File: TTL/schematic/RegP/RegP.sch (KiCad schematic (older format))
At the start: 23 parts, among them U1 74LS153, U10 74LS32, U2 74LS153, U3 74LS175, U4 74LS32, U5 74LS08, U6 74LS08, U8 74LS86, U9 74LS32

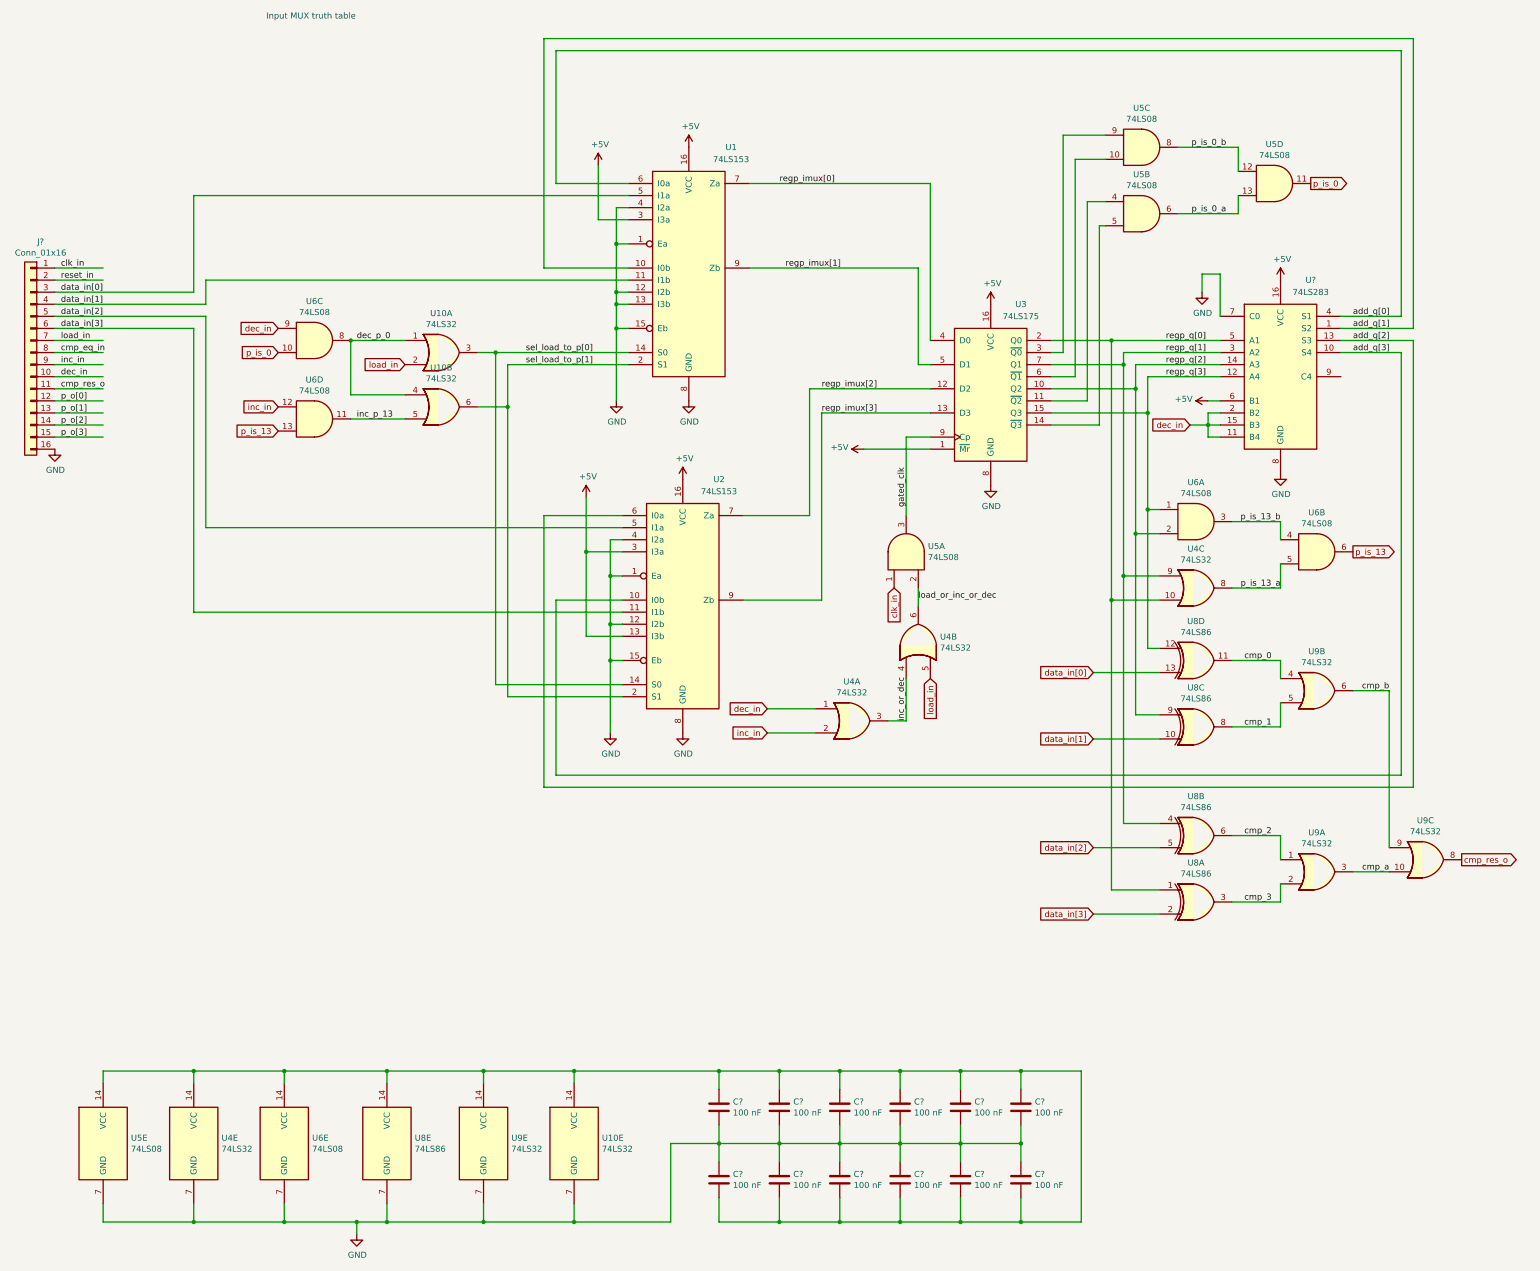
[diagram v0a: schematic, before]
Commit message: Added docu, work in progress schematics and vhdl
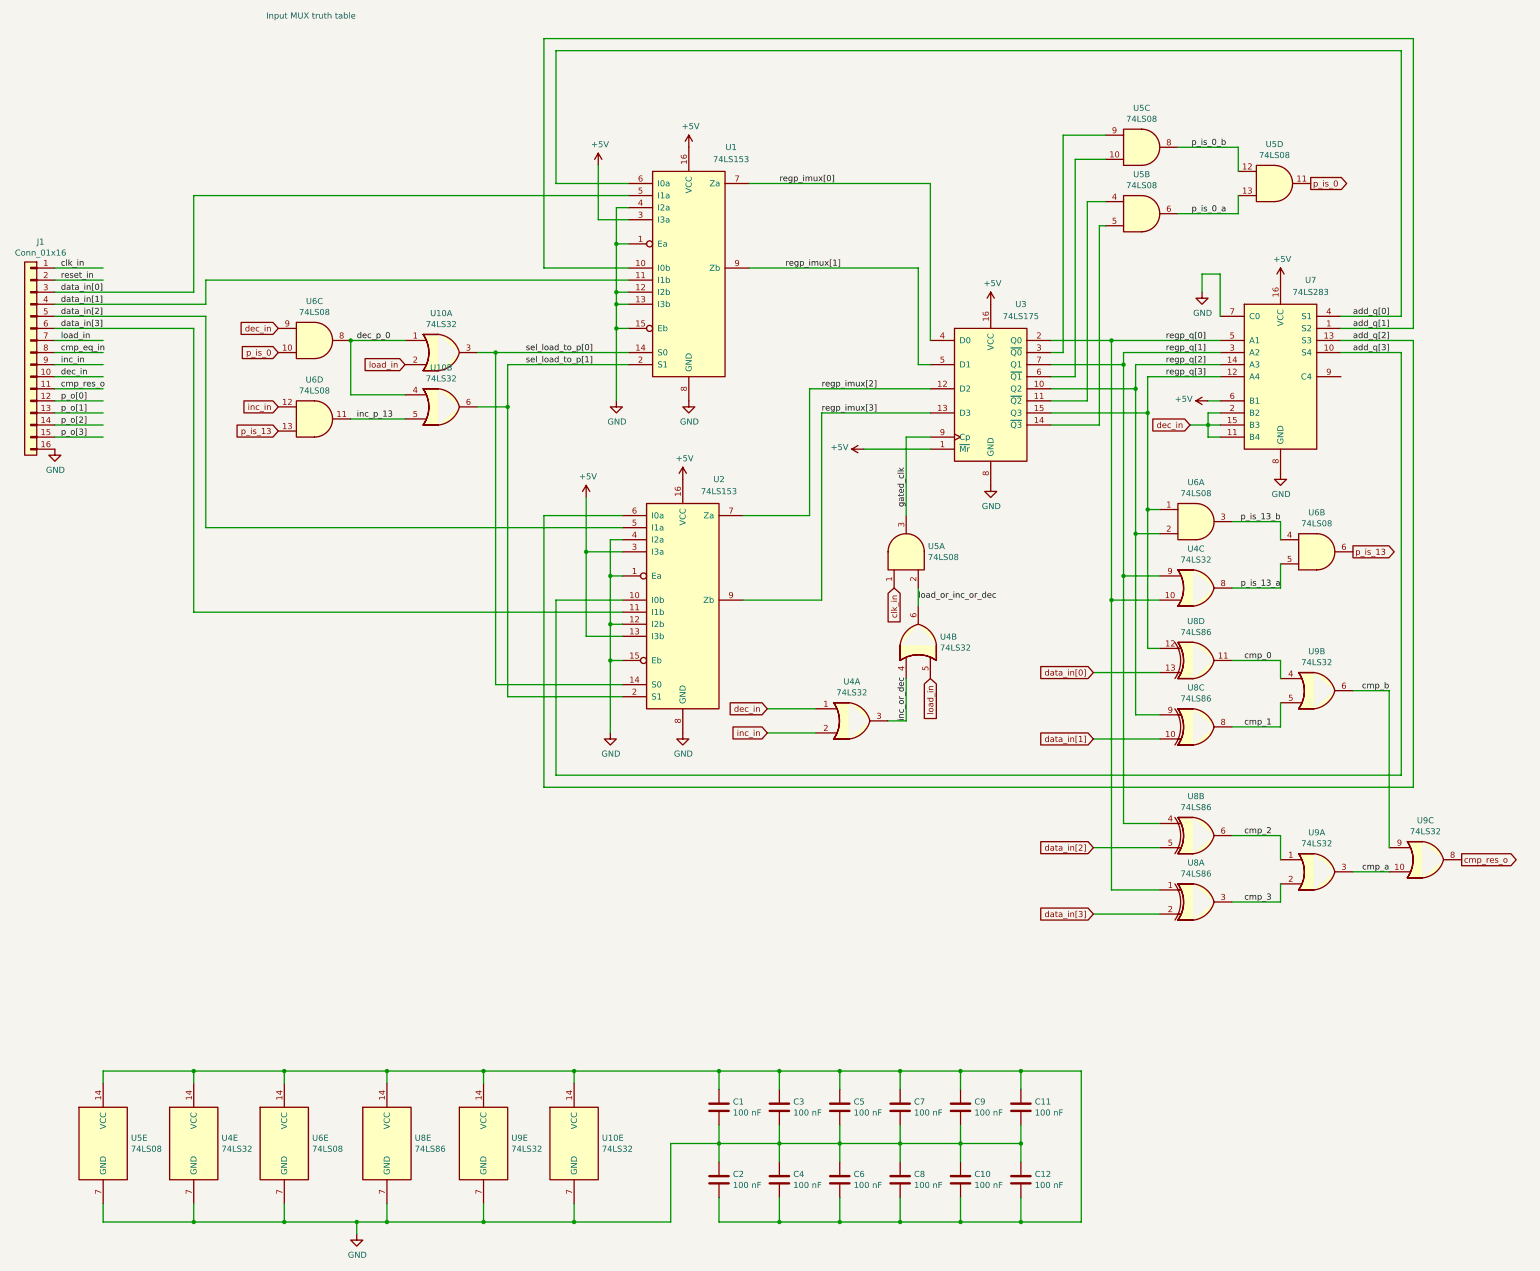
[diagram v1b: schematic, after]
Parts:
- gave numbers to parts that had none: 14
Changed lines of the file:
@@
 $EndComp
 $Comp
-L 74xx:74LS283 U?
+L 74xx:74LS283 U7
 U 1 1 609CD38B
 P 11100 3800
-F 0 "U?" H 11350 4600 50  0000 C CNN
+F 0 "U7" H 11350 4600 50  0000 C CNN
 F 1 "74LS283" H 11350 4500 50  0000 C CNN
 F 2 "" H 11100 3800 50  0001 C CNN
@@
 	10000 3800 10600 3800
 $Comp
-L power:GND #PWR?
+L power:GND #PWR0101
 U 1 1 609CF019
 P 8700 4700
-F 0 "#PWR?" H 8700 4450 50  0001 C CNN
+F 0 "#PWR0101" H 8700 4450 50  0001 C CNN
 F 1 "GND" H 8705 4527 50  0000 C CNN
 F 2 "" H 8700 4700 50  0001 C CNN
@@
 $EndComp
 $Comp
-L power:GND #PWR?
+L power:GND #PWR0102
 U 1 1 609CF0EF
 P 11100 4600
-F 0 "#PWR?" H 11100 4350 50  0001 C CNN
+F 0 "#PWR0102" H 11100 4350 50  0001 C CNN
 F 1 "GND" H 11105 4427 50  0000 C CNN
 F 2 "" H 11100 4600 50  0001 C CNN
@@
 $EndComp
 $Comp
-L power:+5V #PWR?
+L power:+5V #PWR0103
 U 1 1 609D0CA6
 P 8700 3200
-F 0 "#PWR?" H 8700 3050 50  0001 C CNN
+F 0 "#PWR0103" H 8700 3050 50  0001 C CNN
 F 1 "+5V" H 8715 3373 50  0000 C CNN
 F 2 "" H 8700 3200 50  0001 C CNN
@@
 $EndComp
 $Comp
-L power:+5V #PWR?
+L power:+5V #PWR0104
 U 1 1 609D0DA9
 P 11100 3000
-F 0 "#PWR?" H 11100 2850 50  0001 C CNN
+F 0 "#PWR0104" H 11100 2850 50  0001 C CNN
 F 1 "+5V" H 11115 3173 50  0000 C CNN
 F 2 "" H 11100 3000 50  0001 C CNN
@@
 $EndComp
 $Comp
-L power:GND #PWR?
+L power:GND #PWR0105
 U 1 1 609D4985
 P 6200 4000
-F 0 "#PWR?" H 6200 3750 50  0001 C CNN
+F 0 "#PWR0105" H 6200 3750 50  0001 C CNN
 F 1 "GND" H 6205 3827 50  0000 C CNN
 F 2 "" H 6200 4000 50  0001 C CNN
@@
 $EndComp
 $Comp
-L power:GND #PWR?
+L power:GND #PWR0106
 U 1 1 609D4ECC
 P 6150 6750
-F 0 "#PWR?" H 6150 6500 50  0001 C CNN
+F 0 "#PWR0106" H 6150 6500 50  0001 C CNN
 F 1 "GND" H 6155 6577 50  0000 C CNN
 F 2 "" H 6150 6750 50  0001 C CNN
@@
 $EndComp
 $Comp
-L power:+5V #PWR?
+L power:+5V #PWR0107
 U 1 1 609D5502
 P 6150 4650
-F 0 "#PWR?" H 6150 4500 50  0001 C CNN
+F 0 "#PWR0107" H 6150 4500 50  0001 C CNN
 F 1 "+5V" H 6165 4823 50  0000 C CNN
 F 2 "" H 6150 4650 50  0001 C CNN
@@
 $EndComp
 $Comp
-L power:+5V #PWR?
+L power:+5V #PWR0108
 U 1 1 609D5B1E
 P 6200 1900
-F 0 "#PWR?" H 6200 1750 50  0001 C CNN
+F 0 "#PWR0108" H 6200 1750 50  0001 C CNN
 F 1 "+5V" H 6215 2073 50  0000 C CNN
 F 2 "" H 6200 1900 50  0001 C CNN
@@
 p_o[0]
 $Comp
-L Connector_Generic:Conn_01x16 J?
+L Connector_Generic:Conn_01x16 J1
 U 1 1 609F22C6
 P 750 3600
-F 0 "J?" H 668 4517 50  0000 C CNN
+F 0 "J1" H 668 4517 50  0000 C CNN
 F 1 "Conn_01x16" H 668 4426 50  0000 C CNN
 F 2 "" H 750 3600 50  0001 C CNN
@@
 p_o[3]
 $Comp
-L power:GND #PWR?
+L power:GND #PWR0109
 U 1 1 609F7259
 P 950 4400
-F 0 "#PWR?" H 950 4150 50  0001 C CNN
+F 0 "#PWR0109" H 950 4150 50  0001 C CNN
 F 1 "GND" H 955 4227 50  0000 C CNN
 F 2 "" H 950 4400 50  0001 C CNN
@@
 gated_clk
 $Comp
-L power:+5V #PWR?
+L power:+5V #PWR0110
 U 1 1 60A116A1
 P 7650 4400
-F 0 "#PWR?" H 7650 4250 50  0001 C CNN
+F 0 "#PWR0110" H 7650 4250 50  0001 C CNN
 F 1 "+5V" V 7665 4528 50  0000 L CNN
 F 2 "" H 7650 4400 50  0001 C CNN
@@
 load_or_inc_or_dec
 $Comp
-L power:GND #PWR?
+L power:GND #PWR0111
 U 1 1 60A18241
 P 10450 3100
-F 0 "#PWR?" H 10450 2850 50  0001 C CNN
+F 0 "#PWR0111" H 10450 2850 50  0001 C CNN
 F 1 "GND" H 10455 2927 50  0000 C CNN
 F 2 "" H 10450 3100 50  0001 C CNN
@@
 p_is_13
 $Comp
-L power:+5V #PWR?
+L power:+5V #PWR0112
 U 1 1 60A97C7D
 P 10500 4000
-F 0 "#PWR?" H 10500 3850 50  0001 C CNN
+F 0 "#PWR0112" H 10500 3850 50  0001 C CNN
 F 1 "+5V" V 10515 4128 50  0000 L CNN
 F 2 "" H 10500 4000 50  0001 C CNN
@@
 	950  3400 2100 3400
 $Comp
-L power:+5V #PWR?
+L power:+5V #PWR0113
 U 1 1 60BAEDC4
 P 5350 4800
-F 0 "#PWR?" H 5350 4650 50  0001 C CNN
+F 0 "#PWR0113" H 5350 4650 50  0001 C CNN
 F 1 "+5V" H 5365 4973 50  0000 C CNN
 F 2 "" H 5350 4800 50  0001 C CNN
@@
 $EndComp
 $Comp
-L power:GND #PWR?
+L power:GND #PWR0114
 U 1 1 60BAF52D
 P 5600 4000
-F 0 "#PWR?" H 5600 3750 50  0001 C CNN
+F 0 "#PWR0114" H 5600 3750 50  0001 C CNN
 F 1 "GND" H 5605 3827 50  0000 C CNN
 F 2 "" H 5600 4000 50  0001 C CNN
@@
 $EndComp
 $Comp
-L power:GND #PWR?
+L power:GND #PWR0115
 U 1 1 60BAF8CD
 P 5550 6750
-F 0 "#PWR?" H 5550 6500 50  0001 C CNN
+F 0 "#PWR0115" H 5550 6500 50  0001 C CNN
 F 1 "GND" H 5555 6577 50  0000 C CNN
 F 2 "" H 5550 6750 50  0001 C CNN
@@
 	5350 5250 5350 5950
 $Comp
-L power:+5V #PWR?
+L power:+5V #PWR0116
 U 1 1 60C3D20C
 P 5450 2050
-F 0 "#PWR?" H 5450 1900 50  0001 C CNN
+F 0 "#PWR0116" H 5450 1900 50  0001 C CNN
 F 1 "+5V" H 5465 2223 50  0000 C CNN
 F 2 "" H 5450 2050 50  0001 C CNN
@@
 $EndComp
 $Comp
-L power:GND #PWR?
+L power:GND #PWR0117
 U 1 1 60C4CE49
 P 3450 10900
-F 0 "#PWR?" H 3450 10650 50  0001 C CNN
+F 0 "#PWR0117" H 3450 10650 50  0001 C CNN
 F 1 "GND" H 3455 10727 50  0000 C CNN
 F 2 "" H 3450 10900 50  0001 C CNN
@@
 	2100 9550 2850 9550
 $Comp
-L Device:C C?
+L Device:C C1
 U 1 1 60D9291A
 P 6450 9850
-F 0 "C?" H 6565 9896 50  0000 L CNN
+F 0 "C1" H 6565 9896 50  0000 L CNN
 F 1 "100 nF" H 6565 9805 50  0000 L CNN
 F 2 "" H 6488 9700 50  0001 C CNN
@@
 $EndComp
 $Comp
-L Device:C C?
+L Device:C C3
 U 1 1 60D93C61
 P 6950 9850
-F 0 "C?" H 7065 9896 50  0000 L CNN
+F 0 "C3" H 7065 9896 50  0000 L CNN
 F 1 "100 nF" H 7065 9805 50  0000 L CNN
 F 2 "" H 6988 9700 50  0001 C CNN
@@
 $EndComp
 $Comp
-L Device:C C?
+L Device:C C5
 U 1 1 60D93F19
 P 7450 9850
-F 0 "C?" H 7565 9896 50  0000 L CNN
+F 0 "C5" H 7565 9896 50  0000 L CNN
 F 1 "100 nF" H 7565 9805 50  0000 L CNN
 F 2 "" H 7488 9700 50  0001 C CNN
@@
 $EndComp
 $Comp
-L Device:C C?
+L Device:C C7
 U 1 1 60D942D0
 P 7950 9850
-F 0 "C?" H 8065 9896 50  0000 L CNN
+F 0 "C7" H 8065 9896 50  0000 L CNN
 F 1 "100 nF" H 8065 9805 50  0000 L CNN
 F 2 "" H 7988 9700 50  0001 C CNN
@@
 $EndComp
 $Comp
-L Device:C C?
+L Device:C C9
 U 1 1 60D942DA
 P 8450 9850
-F 0 "C?" H 8565 9896 50  0000 L CNN
+F 0 "C9" H 8565 9896 50  0000 L CNN
 F 1 "100 nF" H 8565 9805 50  0000 L CNN
 F 2 "" H 8488 9700 50  0001 C CNN
@@
 $EndComp
 $Comp
-L Device:C C?
+L Device:C C11
 U 1 1 60D942E4
 P 8950 9850
-F 0 "C?" H 9065 9896 50  0000 L CNN
+F 0 "C11" H 9065 9896 50  0000 L CNN
 F 1 "100 nF" H 9065 9805 50  0000 L CNN
 F 2 "" H 8988 9700 50  0001 C CNN
@@
 $EndComp
 $Comp
-L Device:C C?
+L Device:C C2
 U 1 1 60DA075C
 P 6450 10450
-F 0 "C?" H 6565 10496 50  0000 L CNN
+F 0 "C2" H 6565 10496 50  0000 L CNN
 F 1 "100 nF" H 6565 10405 50  0000 L CNN
 F 2 "" H 6488 10300 50  0001 C CNN
@@
 $EndComp
 $Comp
-L Device:C C?
+L Device:C C4
 U 1 1 60DA0766
 P 6950 10450
-F 0 "C?" H 7065 10496 50  0000 L CNN
+F 0 "C4" H 7065 10496 50  0000 L CNN
 F 1 "100 nF" H 7065 10405 50  0000 L CNN
 F 2 "" H 6988 10300 50  0001 C CNN
@@
 $EndComp
 $Comp
-L Device:C C?
+L Device:C C6
 U 1 1 60DA0770
 P 7450 10450
-F 0 "C?" H 7565 10496 50  0000 L CNN
+F 0 "C6" H 7565 10496 50  0000 L CNN
 F 1 "100 nF" H 7565 10405 50  0000 L CNN
 F 2 "" H 7488 10300 50  0001 C CNN
@@
 $EndComp
 $Comp
-L Device:C C?
+L Device:C C8
 U 1 1 60DA077A
 P 7950 10450
-F 0 "C?" H 8065 10496 50  0000 L CNN
+F 0 "C8" H 8065 10496 50  0000 L CNN
 F 1 "100 nF" H 8065 10405 50  0000 L CNN
 F 2 "" H 7988 10300 50  0001 C CNN
@@
 $EndComp
 $Comp
-L Device:C C?
+L Device:C C10
 U 1 1 60DA0784
 P 8450 10450
-F 0 "C?" H 8565 10496 50  0000 L CNN
+F 0 "C10" H 8565 10496 50  0000 L CNN
 F 1 "100 nF" H 8565 10405 50  0000 L CNN
 F 2 "" H 8488 10300 50  0001 C CNN
@@
 $EndComp
 $Comp
-L Device:C C?
+L Device:C C12
 U 1 1 60DA078E
 P 8950 10450
-F 0 "C?" H 9065 10496 50  0000 L CNN
+F 0 "C12" H 9065 10496 50  0000 L CNN
 F 1 "100 nF" H 9065 10405 50  0000 L CNN
 F 2 "" H 8988 10300 50  0001 C CNN
